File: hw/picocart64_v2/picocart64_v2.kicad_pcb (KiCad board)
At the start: 4 copper layers, 100 x 60 mm, 105 parts, among them J1 USB_C_Receptacle_USB2.0, J2 USB_C_Receptacle_USB2.0, J3 Conn_02x06_Odd_Even, J4 Micro_SD_Card_Det, J5 Conn_01x02, J6 Conn_01x06, Q1 FDN340P, SW1 BootButton, SW2 ResetButton, U1 W25Q128JVS, U10 USBLC6-2SC6, U11 AZ1117-3.3, U12 N64-Cartridge, U14 RP2040, U15 RP2040, U16 ESP32-C3-WROOM-02, U2 W25Q128JVS, U3 W25Q128JVS, U4 W25Q128JVS, U5 W25Q128JVS, U6 W25Q128JVS, U7 LY68L6400SLIT, U8 LY68L6400SLIT, U9 SN74LVC138AQDRQ1, Y1 12MHz 10ppm, Y2 12MHz 10ppm

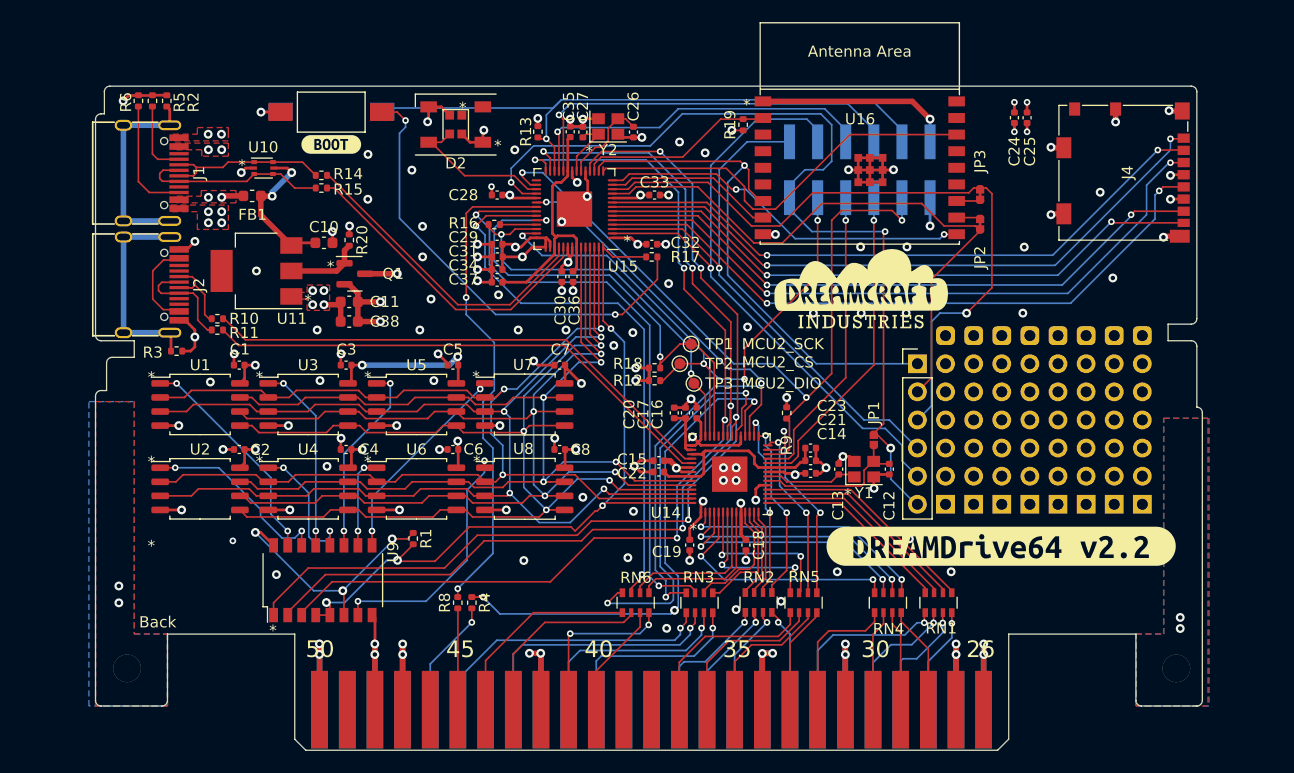
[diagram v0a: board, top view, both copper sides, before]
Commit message: New v2 board revision (v2.2) updated with help from Snipeye. Updated readme.
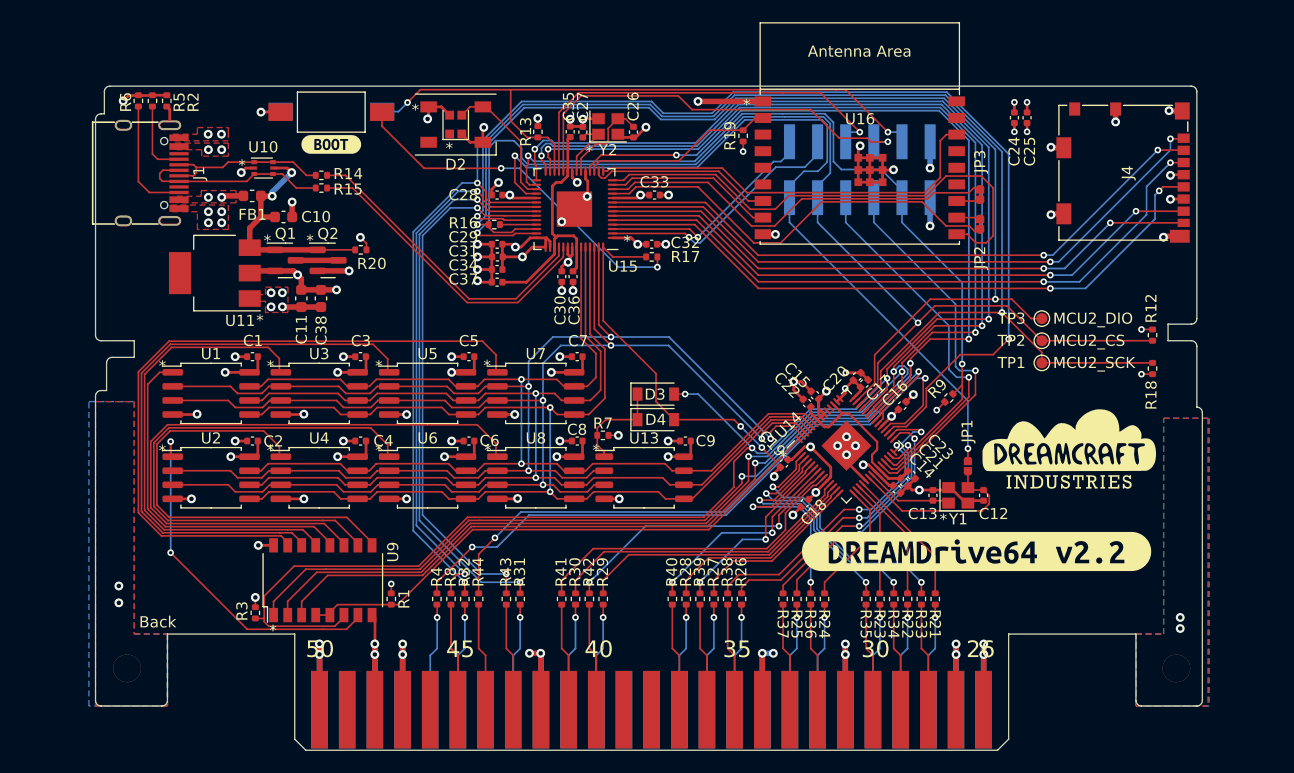
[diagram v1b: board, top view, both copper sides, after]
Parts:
- removed J2: USB_C_Receptacle_USB2.0, Connector_USB_Extra:USB_C_Receptacle_GT-USB-7010
- removed J5: Conn_01x02, project_area:PinHeader_1x08_P2.54mm_Vertical
- removed J6: Conn_01x06, Connector_PinHeader_2.54mm:PinHeader_1x06_P2.54mm_Vertical
- removed R10, R11: 22R, Resistor_SMD:R_0402_1005Metric
- removed RN1, RN2, RN3, RN4, RN5, RN6: 22R_x4, Resistor_SMD:R_Array_Convex_4x0603
- removed kibuzzard-62F95F85: G***, kibuzzard-62F95F85
- added C9: 100n, Capacitor_SMD:C_0402_1005Metric, F.Cu at (153.3, 92.1)
- added D3: D_Small, Diode_SMD:D_SOD-123, F.Cu at (150.6, 87.8)
- added D4: D_Small, Diode_SMD:D_SOD-123, F.Cu at (150.6, 90.1)
- added Q2: FDN340P, Package_TO_SOT_SMD:SOT-23, F.Cu at (121.0, 75.7)
- added R21: 22R, Resistor_SMD:R_0402_1005Metric, F.Cu at (175.9, 106.3)
- added R22: 22R, Resistor_SMD:R_0402_1005Metric, F.Cu at (173.4, 106.3)
- added R23: 22R, Resistor_SMD:R_0402_1005Metric, F.Cu at (170.9, 106.3)
- added R24: 22R, Resistor_SMD:R_0402_1005Metric, F.Cu at (165.9, 106.3)
- added R25: 22R, Resistor_SMD:R_0402_1005Metric, F.Cu at (163.4, 106.3)
- added R26: 22R, Resistor_SMD:R_0402_1005Metric, F.Cu at (158.4, 106.3)
- added R27: 22R, Resistor_SMD:R_0402_1005Metric, F.Cu at (155.9, 106.3)
- added R28: 22R, Resistor_SMD:R_0402_1005Metric, F.Cu at (153.4, 106.3)
- added R29: 22R, Resistor_SMD:R_0402_1005Metric, F.Cu at (145.9, 106.3)
- added R30: 22R, Resistor_SMD:R_0402_1005Metric, F.Cu at (143.4, 106.3)
- added R31: 22R, Resistor_SMD:R_0402_1005Metric, F.Cu at (138.4, 106.3)
- added R32: 22R, Resistor_SMD:R_0402_1005Metric, F.Cu at (133.4, 106.3)
- added R33: 22R, Resistor_SMD:R_0402_1005Metric, F.Cu at (174.6, 106.3)
- added R34: 22R, Resistor_SMD:R_0402_1005Metric, F.Cu at (172.1, 106.3)
- added R35: 22R, Resistor_SMD:R_0402_1005Metric, F.Cu at (169.6, 106.3)
- added R36: 22R, Resistor_SMD:R_0402_1005Metric, F.Cu at (164.6, 106.3)
- added R37: 22R, Resistor_SMD:R_0402_1005Metric, F.Cu at (162.1, 106.3)
- added R38: 22R, Resistor_SMD:R_0402_1005Metric, F.Cu at (157.1, 106.3)
- added R39: 22R, Resistor_SMD:R_0402_1005Metric, F.Cu at (154.6, 106.3)
- added R40: 22R, Resistor_SMD:R_0402_1005Metric, F.Cu at (152.1, 106.3)
- added R41: 22R, Resistor_SMD:R_0402_1005Metric, F.Cu at (142.1, 106.3)
- added R42: 22R, Resistor_SMD:R_0402_1005Metric, F.Cu at (144.6, 106.3)
- added R43: 22R, Resistor_SMD:R_0402_1005Metric, F.Cu at (137.1, 106.3)
- added R44: 22R, Resistor_SMD:R_0402_1005Metric, F.Cu at (134.6, 106.3)
- added R7: 100K, Resistor_SMD:R_0402_1005Metric, F.Cu at (145.8, 91.5)
- added U13: W25Q128JVS, Package_SO:SOIC-8_5.23x5.23mm_P1.27mm, F.Cu at (149.6, 95.4)
- R3: value 100k -> 10K
- U7, U8: value LY68L6400SLIT -> W25Q128JVS; footprint Package_SO:SOIC-8_5.275x5.275mm_P1.27mm -> Package_SO:SOIC-8_5.23x5.23mm_P1.27mm
- moved R12 45.2 mm to (195.5, 82.5), turned to 90 degrees
- moved R18 45.0 mm to (195.5, 85.5), turned to 90 degrees
- moved TP2 32.8 mm to (185.5, 83.0)
- moved TP3 32.0 mm to (185.5, 81.0)
- moved TP1 31.7 mm to (185.5, 85.0)
- moved R3 24.7 mm to (114.4, 107.6), turned to -90 degrees
- moved G*** 23.7 mm to (187.9, 93.2)
- moved C16 18.6 mm to (172.9, 88.9), turned to 45 degrees
- moved C20 16.8 mm to (168.8, 86.2), turned to 45 degrees
- moved C17 16.4 mm to (169.5, 86.9), turned to 45 degrees
- moved C15 15.3 mm to (165.0, 87.9), turned to 135 degrees
- moved C22 14.8 mm to (164.3, 88.6), turned to 135 degrees
- moved R9 14.7 mm to (177.1, 88.2), turned to 45 degrees
- moved C19 11.3 mm to (162.2, 94.1), turned to -135 degrees
- moved U14 10.9 mm to (167.8, 92.5), turned to 45 degrees
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- renumbered SW2 to RESET
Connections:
- Q1 pad 1: /Mainboard/3V3_USB -> VBUS
- Q1 pad 3: /Mainboard/N64_VCC -> Net-(Q1-Pad3)
- R20 pad 2: /Mainboard/3V3_USB -> VBUS
- R3 pad 2: Net-(J2-PadS1) -> /Mainboard/DEMUX_IE
- U1 pad 1: /PSRAM Array/CS1 -> /PSRAM Array/CS4
- U11 pad 2: /Mainboard/3V3_USB -> +3V3
- U14 pad 46: Net-(R10-Pad2) -> unconnected-(U14-Pad46)
- U14 pad 47: Net-(R11-Pad2) -> unconnected-(U14-Pad47)
- U2 pad 1: /PSRAM Array/CS2 -> /PSRAM Array/CS8
- U4 pad 1: /PSRAM Array/CS5 -> /PSRAM Array/CS7
- U5 pad 1: /PSRAM Array/CS4 -> /PSRAM Array/CS2
- U7 pad 1: /PSRAM Array/CS7 -> /PSRAM Array/CS1
- U8 pad 1: /PSRAM Array/CS8 -> /PSRAM Array/CS5
- U9 pad 6: +3V3 -> /Mainboard/DEMUX_IE
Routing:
- net +3V3: track 437.0 -> 116.1 mm, vias 33 -> 35
- net /Mainboard/DEMUX_IE: track 0.00 -> 165.0 mm, vias 0 -> 5
- net /Mainboard/~{COLD_RESET}: track 60.5 -> 137.3 mm
- net /Mainboard/MCU2_SCK: track 43.4 -> 111.6 mm
- net /Mainboard/MCU2_DIO: track 36.2 -> 100.3 mm
- net /Mainboard/DEMUX_A2: track 89.2 -> 143.8 mm
- net /Mainboard/DEMUX_A1: track 92.3 -> 141.2 mm
- net /Mainboard/DEMUX_A0: track 89.1 -> 137.4 mm
- net Net-(R10-Pad2): track 47.6 -> 0.00 mm
- net Net-(R11-Pad2): track 47.3 -> 0.00 mm
- net /PSRAM Array/CS5: track 12.6 -> 58.7 mm, vias 2 -> 0
- net /Mainboard/MCU2_CS: track 57.8 -> 103.2 mm, vias 4 -> 2
- net /PSRAM Array/CS1: track 20.3 -> 63.1 mm, vias 2 -> 0
- net /PSRAM Array/CS6: track 8.38 -> 49.4 mm, vias 2 -> 0
- net /Mainboard/MCU2_UART_TX: track 60.1 -> 23.3 mm
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- added copper zone on In2.Cu, net +3V3
- added copper zone on In2.Cu, net /Mainboard/VBUS'
- removed copper zone on In1.Cu, net /Mainboard/VBUS'
- removed copper zone on In2.Cu, net GND
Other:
- rule pad_to_mask_clearance: 0.13 -> 0
- board text removed: "ESP32_D0_TX / MCU2_GPIO08"
- board text removed: "ESP32_D1_RX / MCU2_GPIO09"
- board text removed: "ESP32_SCK / MCU2_GPIO13"
- board text removed: "MCU2_UART_RX / MCU2_GPIO01"
- board text removed: "MCU2_UART_TX / MCU2_GPIO00"

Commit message: Updated v2 pcb to use a tristate buffer to toggle between boot flash and psram array.
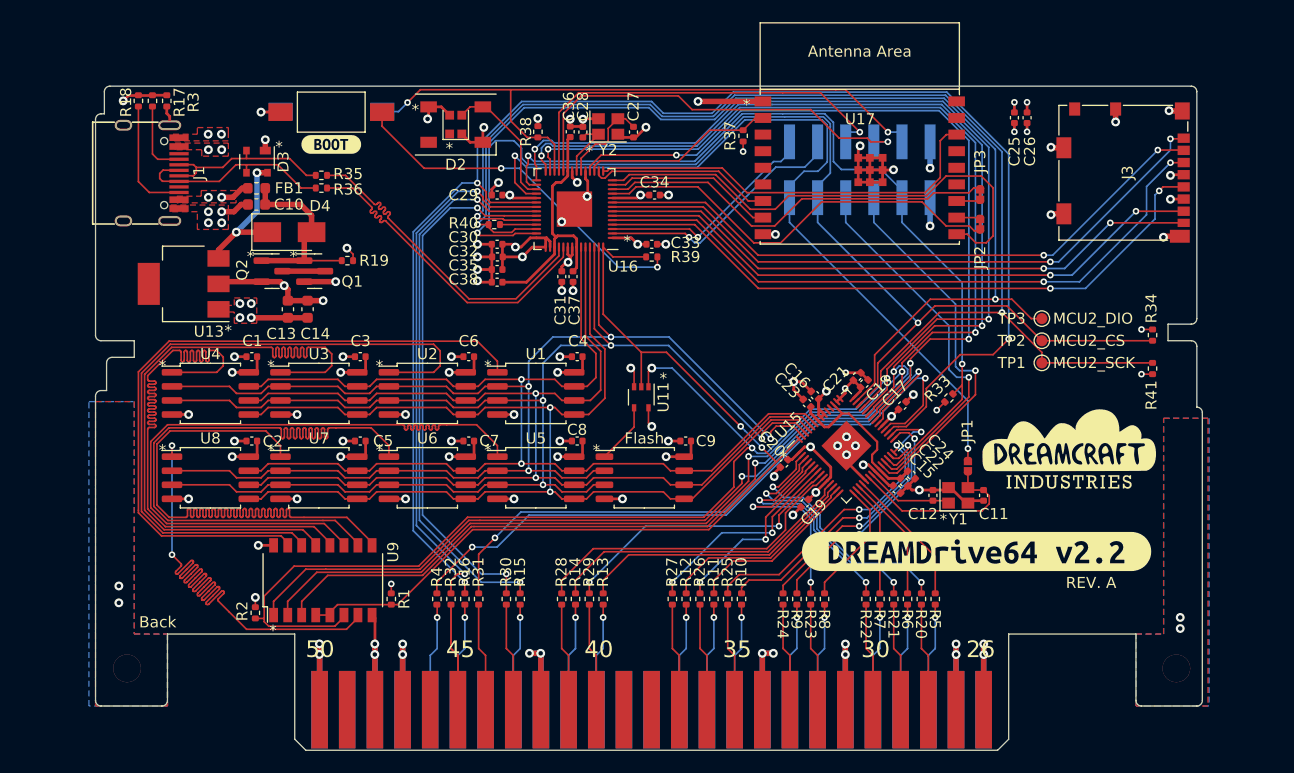
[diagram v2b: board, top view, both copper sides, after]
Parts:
- removed the R7 at (145.8, 91.5)
- removed U10: USBLC6-2SC6, Package_TO_SOT_SMD:SOT-666
- added U11: NC7SZ125M5X, Package_TO_SOT_SMD:SOT-353_SC-70-5, F.Cu at (149.3, 88.1)
- D3: value D_Small -> DRTR5V0U2SR-7; footprint Diode_SMD:D_SOD-123 -> Package_TO_SOT_SMD:SOT-143
- D4: footprint Diode_SMD:D_SOD-123 -> Diode_SMD:D_SMA
- R19: renamed from R20; value 100k -> 10k
- moved D3 41.7 mm to (114.6, 66.8), turned to -90 degrees
- moved D4 37.2 mm to (117.5, 73.2)
- moved U13 2.98 mm to (108.0, 77.9)
- moved C10 2.69 mm to (114.5, 70.7), turned to 180 degrees
- moved Q1 1.55 mm to (119.8, 76.7)
- moved Q2 1.55 mm to (115.9, 76.7)
- moved C13 1.55 mm to (117.4, 80.2)
- moved C14 1.55 mm to (119.2, 80.2)
- moved R19 1.55 mm to (122.8, 75.8)
- moved FB1 0.80 mm to (114.5, 69.2)
- moved C1 0.06 mm to (114.1, 84.4)
- moved C2 0.06 mm to (114.1, 92.1)
- moved U4 0.06 mm to (110.4, 87.8)
- moved U8 0.06 mm to (110.4, 95.4)
- renumbered C12 to C11, C13 to C12, C11 to C13, C38 to C14, C14 to C15, C15 to C16, C16 to C17, C17 to C18, C18 to C19, C19 to C20, C20 to C21, C21 to C22, C22 to C23, C23 to C24, C24 to C25, C25 to C26, C26 to C27, C27 to C28, C28 to C29, C29 to C30, C30 to C31, C31 to C32, C32 to C33, C33 to C34, C34 to C35, C35 to C36, C36 to C37, C37 to C38, C7 to C4, C4 to C5, C5 to C6, C6 to C7, U13 to Flash, J3 to J2, J4 to J3, Q2 to Q1, Q1 to Q2, R26 to R10, R27 to R11, R28 to R12, R29 to R13, R30 to R14, R31 to R15, R32 to R16, R5 to R17, R6 to R18, R3 to R2, R33 to R20, R34 to R21, R35 to R22, R36 to R23, R37 to R24, R38 to R25, R39 to R26, R40 to R27, R41 to R28, R42 to R29, R2 to R3, R43 to R30, R44 to R31, R8 to R32, R9 to R33, R12 to R34, R14 to R35, R15 to R36, R19 to R37, R13 to R38, R17 to R39, R16 to R40, R18 to R41, R21 to R5, R22 to R6, R23 to R7, R24 to R8, R25 to R9, RESET to SW2, U7 to U1, U11 to U13, U12 to U14, U14 to U15, U15 to U16, U16 to U17, U5 to U2, U1 to U4, U8 to U5, U4 to U7, U2 to U8
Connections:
- D3 pad 1: /PSRAM Array/CSBOOT -> GND
- D3 pad 2: /Mainboard/DEMUX_IE -> /Mainboard/MCU2_USB_D-
- D4 pad 1: /PSRAM Array/CSBOOT -> Net-(D3-Pad4)
- D4 pad 2: ~{SSI_CS} -> VBUS
- U13 pad 3: VBUS -> Net-(D3-Pad4)
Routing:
- net /PSRAM Array/CS4: track 31.8 -> 62.6 mm
- net /PSRAM Array/CS8: track 31.9 -> 59.6 mm
- net /PSRAM Array/CS7: track 39.6 -> 62.5 mm
- net /PSRAM Array/CS3: track 44.0 -> 62.8 mm
- net /PSRAM Array/CS6: track 49.4 -> 63.0 mm
- net Net-(D3-Pad4): track 0.00 -> 12.9 mm, vias 0 -> 2
- net /PSRAM Array/CS2: track 53.5 -> 62.9 mm
- net /Mainboard/DEMUX_IE: track 165.0 -> 169.8 mm
- net /PSRAM Array/CS5: track 58.7 -> 62.8 mm
- net VBUS: track 21.4 -> 17.7 mm, vias 2 -> 0
- net /PSRAM Array/CSBOOT: track 9.11 -> 5.53 mm
- net Net-(R35-Pad2): track 28.0 -> 29.9 mm
- net Net-(R36-Pad2): track 28.2 -> 29.9 mm
- net /Mainboard/N64_VCC: track 90.7 -> 92.3 mm
- net /Mainboard/MCU2_USB_D+: track 17.5 -> 18.9 mm
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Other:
- board text added: "REV. A"

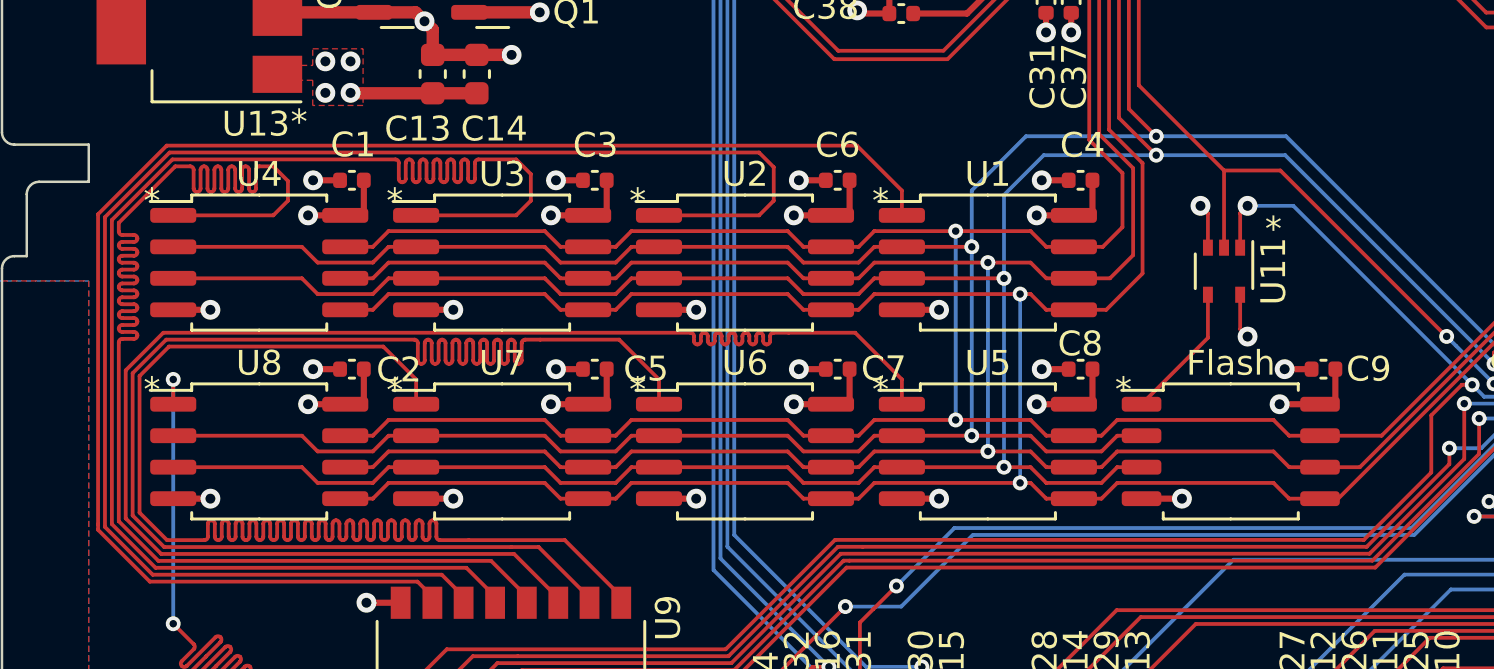
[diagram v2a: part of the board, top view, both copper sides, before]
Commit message: Updated schematic to use correct footprints for the psram. Also updated the components and datasheets for the tristate buffer and psram.
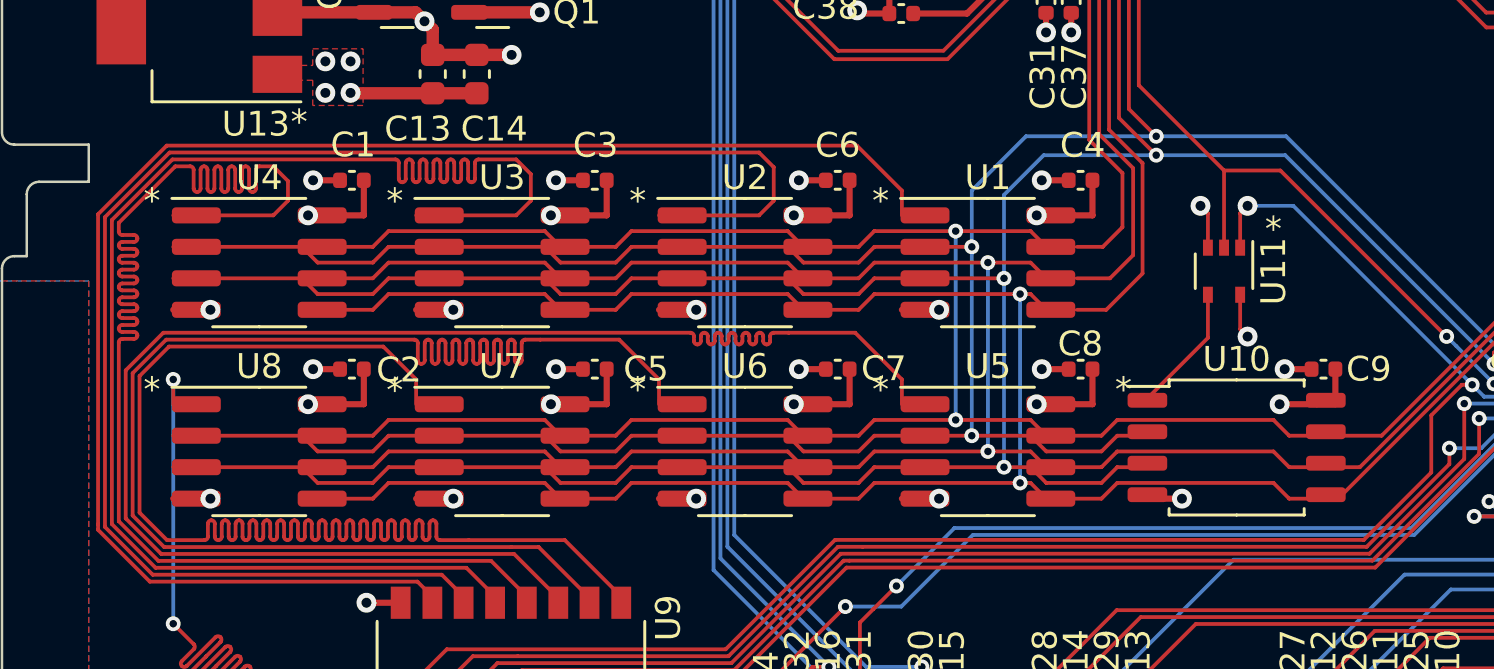
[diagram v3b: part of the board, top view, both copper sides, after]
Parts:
- removed Flash: W25Q128JVS, Package_SO:SOIC-8_5.23x5.23mm_P1.27mm
- added U10: W25Q128JVS, Package_SO:SOIC-8_5.23x5.23mm_P1.27mm, F.Cu at (149.8, 95.2)
- U1, U2, U3, U4, U5, U6, U7, U8: value W25Q128JVS -> APS6404L-3SQR; footprint Package_SO:SOIC-8_5.23x5.23mm_P1.27mm -> Package_SO:SOP-8_3.76x4.96mm_P1.27mm
- U11: value NC7SZ125M5X -> 74LVC1G125GW
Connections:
- U2 pad 1: /PSRAM Array/CS2 -> /PSRAM Array/CS1
- U3 pad 1: /PSRAM Array/CS3 -> /PSRAM Array/CS1
- U4 pad 1: /PSRAM Array/CS4 -> /PSRAM Array/CS1
- U5 pad 1: /PSRAM Array/CS5 -> /PSRAM Array/CS1
- U6 pad 1: /PSRAM Array/CS6 -> /PSRAM Array/CS1
- U7 pad 1: /PSRAM Array/CS7 -> /PSRAM Array/CS1
- U8 pad 1: /PSRAM Array/CS8 -> /PSRAM Array/CS1
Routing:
- net /PSRAM Array/CS1: track 62.9 -> 251.2 mm
- net /Mainboard/SSI_SCLK: track 110.5 -> 236.3 mm, vias 2 -> 6
- net /Mainboard/SSI_SD2: track 125.9 -> 0.00 mm, vias 4 -> 0
- net /Mainboard/SSI_SD1: track 124.1 -> 0.00 mm, vias 4 -> 0
- net /Mainboard/SSI_SD3: track 108.7 -> 232.8 mm, vias 2 -> 6
- net /PSRAM Array/CS2: track 62.9 -> 0.00 mm
- net /PSRAM Array/CS5: track 62.8 -> 0.00 mm
- net /PSRAM Array/CS7: track 62.5 -> 0.00 mm
